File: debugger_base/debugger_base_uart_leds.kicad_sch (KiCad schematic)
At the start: 16 parts, among them SW2 UART CHx LED enable switch

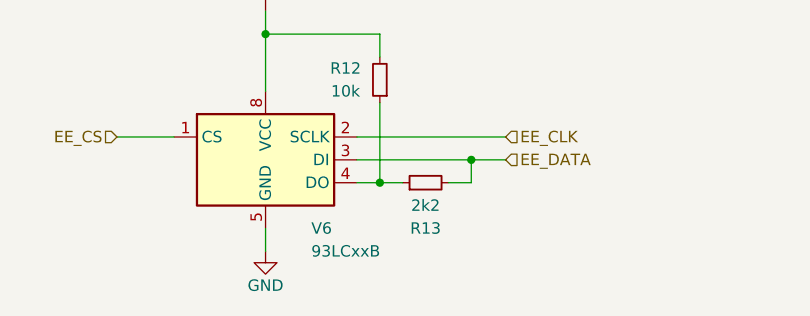
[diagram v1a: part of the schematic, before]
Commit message: decrease clearance of copper pours
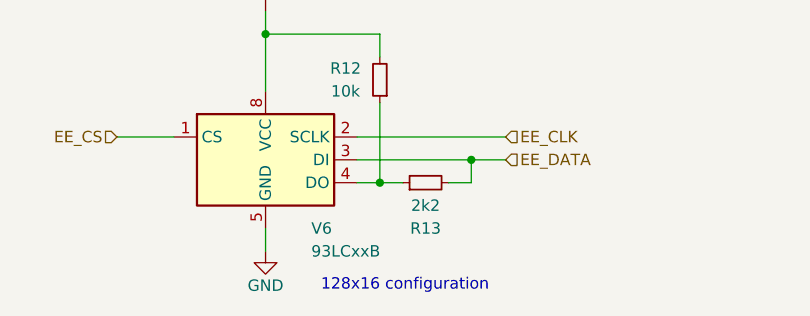
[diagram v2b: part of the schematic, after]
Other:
- note added: "128x16 configuration"
- title: (none) -> FT4232 Debugger Base
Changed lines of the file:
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@@
 	(generator_version "8.0")
 	(paper "A4")
+	(title_block
+		(title "FT4232 Debugger Base")
+		(date "2024-02-10")
+		(rev "v1.0")
+		(comment 4 "Simon Brenninger")
+	)
 	(junction
 		(at 73.66 50.8)
@@
 		)
 	)
+	(text "128x16 configuration"
+		(exclude_from_sim no)
+		(at 137.414 125.73 0)
+		(effects
+			(font
+				(size 1.27 1.27)
+			)
+		)
+	)
 	(label "ChanB_EN"
 		(at 172.72 58.42 0)
-		(fields_autoplaced yes)
 		(effects
 			(font
@@
 	(label "ChanA_EN"
 		(at 172.72 55.88 0)
-		(fields_autoplaced yes)
 		(effects
 			(font
@@
 	(label "ChanC_EN"
 		(at 172.72 60.96 0)
-		(fields_autoplaced yes)
 		(effects
 			(font
@@
 	(label "ChanD_EN"
 		(at 172.72 63.5 0)
-		(fields_autoplaced yes)
 		(effects
 			(font
@@
 		(shape input)
 		(at 38.1 58.42 0)
-		(fields_autoplaced yes)
 		(effects
 			(font
@@
 		(shape input)
 		(at 109.22 63.5 180)
-		(fields_autoplaced yes)
 		(effects
 			(font
@@
 		(shape input)
 		(at 105.41 109.22 180)
-		(fields_autoplaced yes)
 		(effects
 			(font
@@
 		(shape input)
 		(at 109.22 50.8 180)
-		(fields_autoplaced yes)
 		(effects
 			(font
@@
 		(shape input)
 		(at 38.1 54.61 0)
-		(fields_autoplaced yes)
 		(effects
 			(font
@@
 		(shape input)
 		(at 148.59 109.22 0)
-		(fields_autoplaced yes)
 		(effects
 			(font
@@
 		(shape input)
 		(at 109.22 66.04 180)
-		(fields_autoplaced yes)
 		(effects
 			(font
@@
 		(shape input)
 		(at 148.59 111.76 0)
-		(fields_autoplaced yes)
 		(effects
 			(font
@@
 		(shape input)
 		(at 109.22 55.88 180)
-		(fields_autoplaced yes)
-		(effects
-			(font
+		(effects
+			(font
